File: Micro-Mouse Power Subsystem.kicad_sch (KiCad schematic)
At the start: 12 parts, among them J1 Pin Header

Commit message: This was just a check to see that everything is working
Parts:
- removed R1: R, symbol Device:R
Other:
- note added: "This is just a check that my GitHub Repo works as it should"
- note removed: "What the hell is going on with github"
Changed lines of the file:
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@@
     (effects (font (size 1.5 1.5) (color 0 0 0 1)) (justify left bottom))
   )
-  (text "What the hell is going on with github" (at 36.83 134.62 0)
+  (text "This is just a check that my GitHub Repo works as it should"
+    (at 36.83 134.62 0)
     (effects (font (size 1.27 1.27)) (justify left bottom))
   )
@@
         )
       )
-    )
-  )
-  (symbol (lib_id "Device:R") (at 82.55 179.705 0) (unit 1)
-    (in_bom yes) (on_board yes) (dnp no) (fields_autoplaced)
-    (property "Reference" "R1" (at 85.09 178.435 0)
-      (effects (font (size 1.27 1.27)) (justify left))
-    )
-    (property "Value" "R" (at 85.09 180.975 0)
-      (effects (font (size 1.27 1.27)) (justify left))
-    )
-    (property "Footprint" "" (at 80.772 179.705 90)
-      (effects (font (size 1.27 1.27)) hide)
-    )
-    (property "Datasheet" "~" (at 82.55 179.705 0)
-      (effects (font (size 1.27 1.27)) hide)
-    )
-    (pin "2")
-    (pin "1")
-    (instances
-      (project "Micro-Mouse Power Subsystem"
-        (path "/b84c8230-4cbd-48ad-931b-8b6e428e7801"
-          (reference "R1") (unit 1)
-        )
-      )

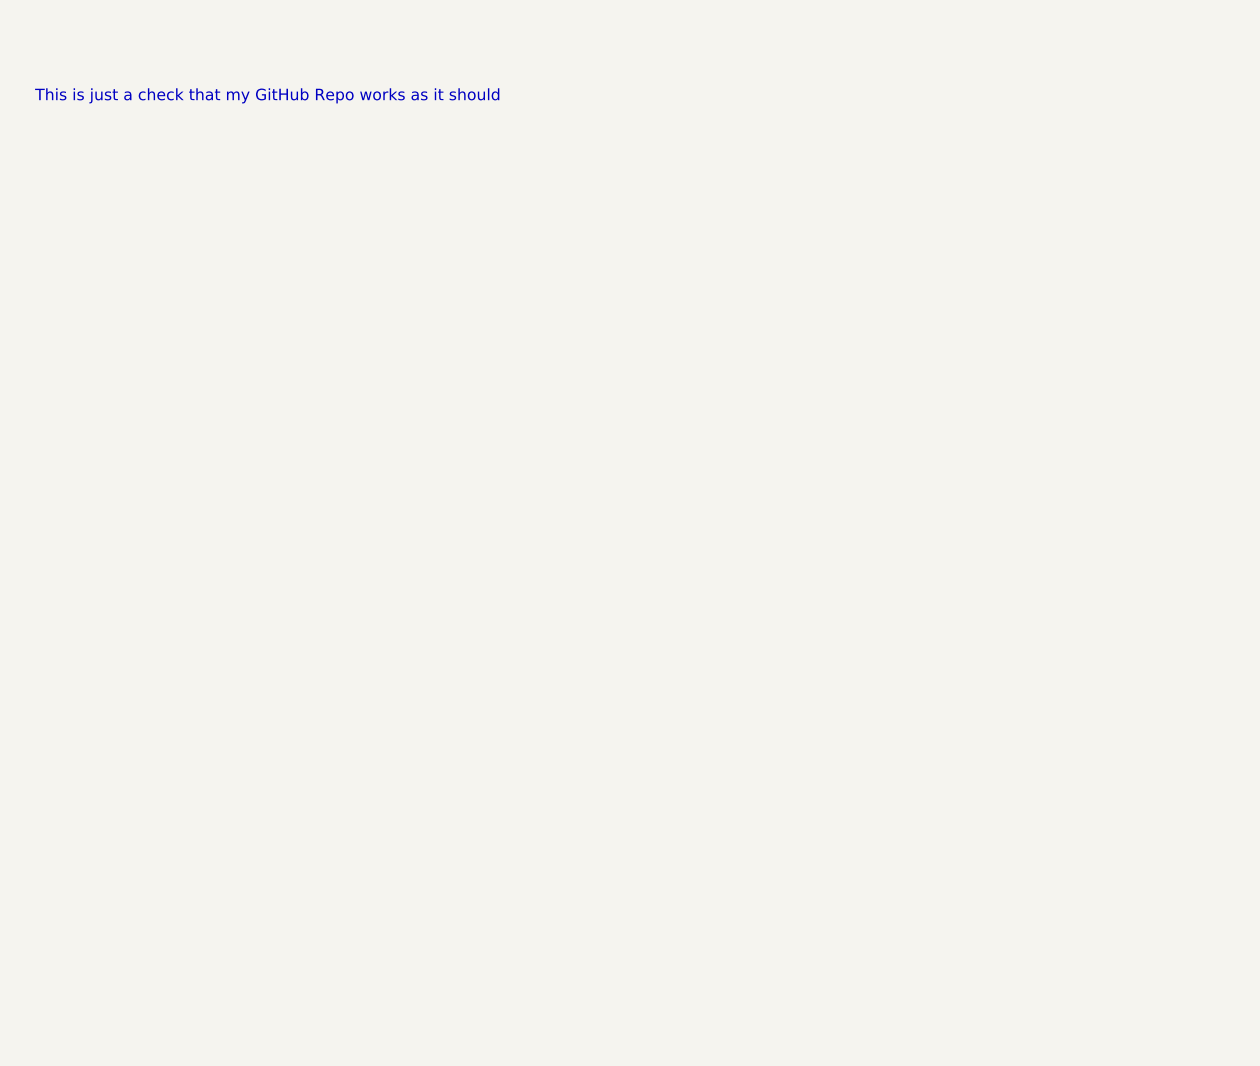
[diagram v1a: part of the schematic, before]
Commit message: Added the Battery Charging Circuit and footprints
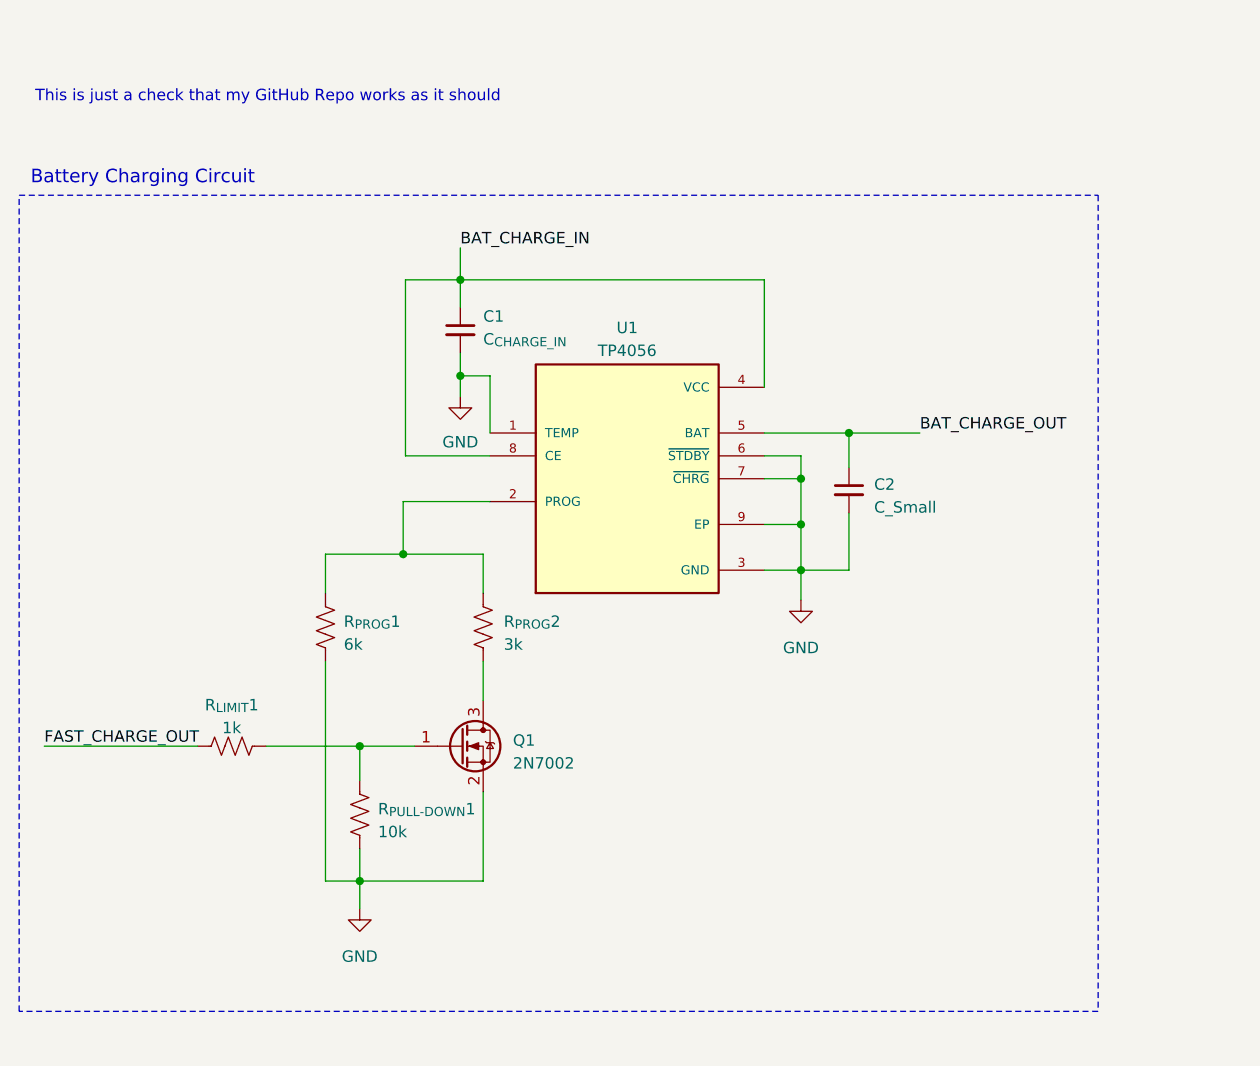
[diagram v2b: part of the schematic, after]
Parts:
- added C1: C_{CHARGE_IN}, Capacitor_SMD:C_0603_1608Metric, symbol Device:C_Small
- added C2: C_Small, Capacitor_SMD:C_0603_1608Metric, symbol Device:C_Small
- added Q1: 2N7002, Package_TO_SOT_SMD:SOT-23, symbol Transistor_FET:2N7002
- added R_{LIMIT}1: 1k, Resistor_SMD:R_0603_1608Metric, symbol Device:R_US
- added R_{PROG}1: 6k, Resistor_SMD:R_0603_1608Metric, symbol Device:R_US
- added R_{PROG}2: 3k, Resistor_SMD:R_0603_1608Metric, symbol Device:R_US
- added R_{PULL-DOWN}1: 10k, Resistor_SMD:R_0603_1608Metric, symbol Device:R_US
- added U1: TP4056, Imports:SOP127P600X175-9N, symbol TP4056:TP4056
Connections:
- net GND: now also C1.2, C2.2, Q1.2 (S), R_{PROG}1.2, R_{PULL-DOWN}1.2, U1.1 (TEMP), U1.3 (GND), U1.6 (~{STDBY}), U1.7 (~{CHRG}), U1.9 (EP)
- new net: R_{PROG}1.1, R_{PROG}2.1, U1.2 (PROG)
- new net: Q1.1 (G), R_{LIMIT}1.2, R_{PULL-DOWN}1.1
- new net: Q1.3 (D), R_{PROG}2.2
- new net BAT_CHARGE_IN: C1.1, U1.4 (VCC), U1.8 (CE)
- new net BAT_CHARGE_OUT: C2.1, U1.5 (BAT)
- new net FAST_CHARGE_OUT: R_{LIMIT}1.1
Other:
- note added: "Battery Charging Circuit"

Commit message: start of motor
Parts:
- added C3: 0.01uF, symbol Device:C
- added C4: 10uF, symbol Device:C_Polarized
- added R1: 200m, symbol Device:R_US
- added U2: DRV8833PWP, Package_SO:HTSSOP-16-1EP_4.4x5mm_P0.65mm_EP3.4x5mm_Mask2.46x2.31mm_ThermalVias, symbol Driver_Motor:DRV8833PWP
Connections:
- net GND: now also C4.2, R1.2, U2.13 (GND), U2.17 (GND(PPAD))
- new net: R1.1, U2.3 (AISEN), U2.6 (BISEN)
- new net: C3.2, U2.11 (VCP)
- new net 5V_From_Regulator: C3.1, C4.1, U2.12 (VM)
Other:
- note removed: "This is just a check that my GitHub Repo works as it should"
